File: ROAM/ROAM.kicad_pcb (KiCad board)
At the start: 4 copper layers, 90 x 56.8 mm, 26 parts, among them J1 CommanderX16Expansion Alt, SW1 SW_DIP_x04, U1 SST39SF040 (ROM), U2 74HCT00, U3 74HCT138, U4 AS6C4008 (RAM), U5 FM24C64B

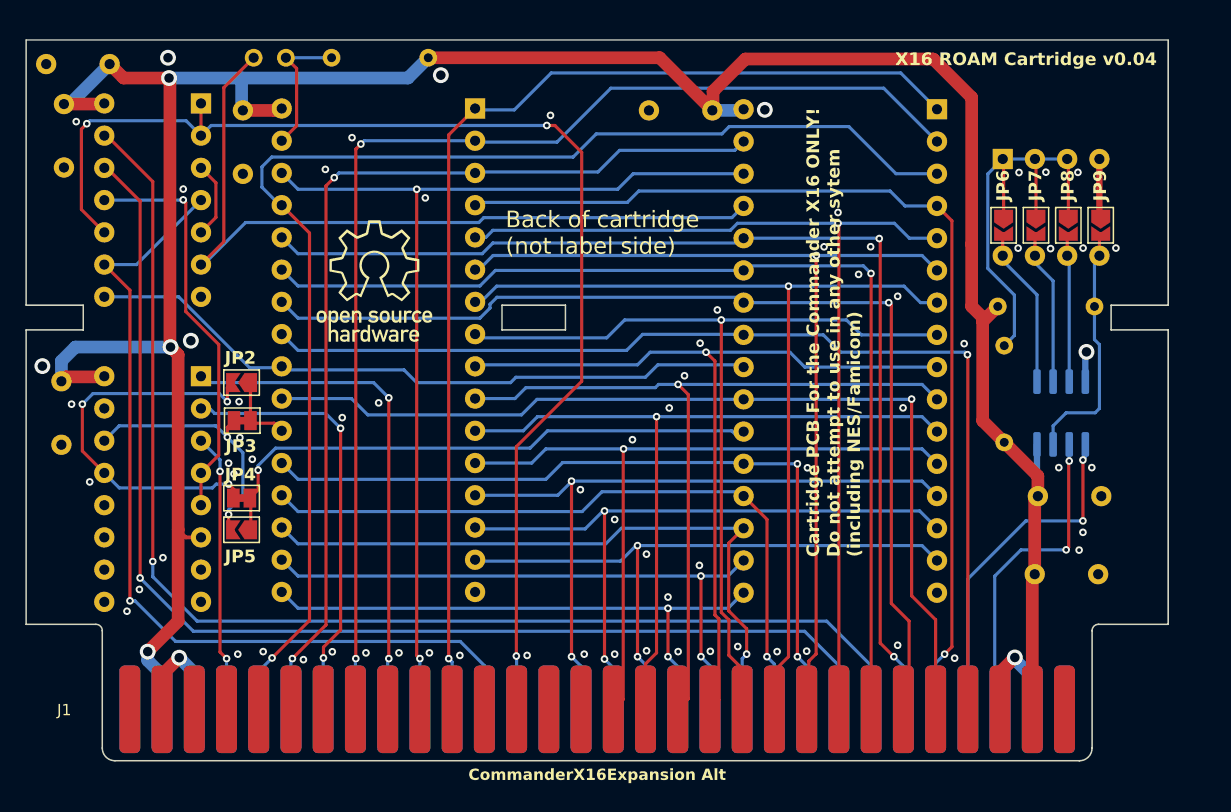
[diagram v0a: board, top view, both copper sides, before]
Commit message: Routed new layout with larger footprint keepout zones.
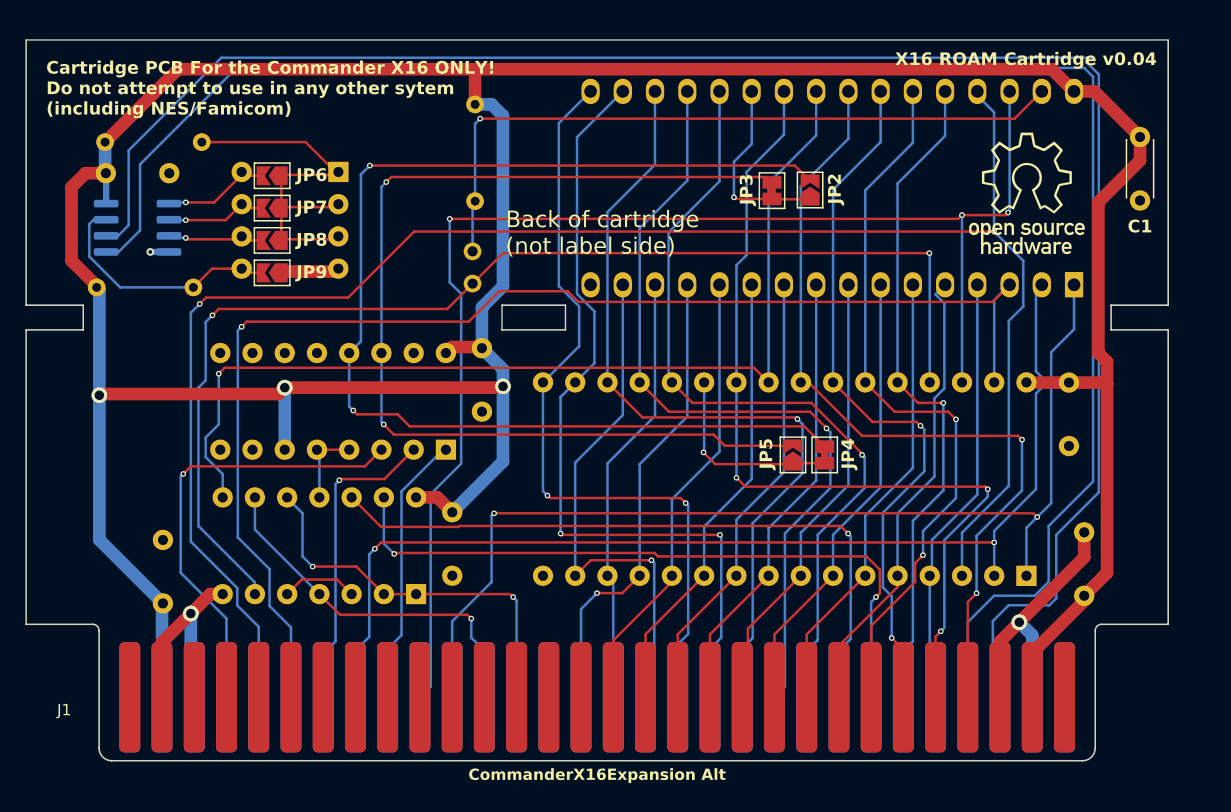
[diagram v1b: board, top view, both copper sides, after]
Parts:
- C1: moved to F.Cu
- U1: footprint Package_DIP:DIP-32_W15.24mm_Socket -> Socket:DIP_Socket-32_W11.9_W12.7_W15.24_W17.78_W18.5_3M_232-1285-00-0602J
- U2: footprint Package_DIP:DIP-14_W7.62mm_Socket -> Package_DIP:DIP-14_W7.62mm
- U3: footprint Package_DIP:DIP-16_W7.62mm_Socket -> Package_DIP:DIP-16_W7.62mm
- moved C7 89.7 mm to (130.8, 116.8), turned to -90 degrees
- moved C5 77.7 mm to (58.7, 88.5)
- moved R2 74.7 mm to (53.6, 86.0), turned to 0 degrees
- moved U5 74.2 mm to (56.2, 92.8), turned to 180 degrees
- moved C6 73.7 mm to (58.2, 117.4), turned to -90 degrees
- moved R3 71.0 mm to (60.6, 97.5)
- moved C1 70.7 mm to (135.2, 90.7)
- moved JP9 65.4 mm to (66.8, 96.3), turned to 180 degrees
- moved JP8 62.8 mm to (66.8, 93.8), turned to 180 degrees
- moved JP7 60.2 mm to (66.8, 91.2), turned to 180 degrees
- moved JP6 57.8 mm to (66.8, 88.7), turned to 180 degrees
- moved SW1 52.4 mm to (72.0, 88.4), turned to 180 degrees
- moved U1 49.2 mm to (130.0, 97.3), turned to 90 degrees
- moved JP2 47.3 mm to (109.2, 89.8), turned to 90 degrees
- moved JP4 46.1 mm to (110.3, 110.7), turned to -90 degrees
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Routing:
- net /SCL: track 25.0 -> 143.4 mm, vias 2 -> 0
- net /SDA: track 27.3 -> 142.0 mm, vias 2 -> 0
- net /RWB: track 98.9 -> 31.1 mm, vias 3 -> 2
- net +5V: track 211.7 -> 275.1 mm
- net Net-(JP2-B): track 31.1 -> 93.6 mm, vias 3 -> 2
- net Net-(JP3-A): track 20.6 -> 83.0 mm
- net /A14: track 99.2 -> 54.0 mm, vias 1 -> 2
- net Net-(JP1-B): track 11.0 -> 55.9 mm, vias 0 -> 1
- net A12: track 77.7 -> 34.3 mm, vias 1 -> 0
- net /PHI2: track 70.6 -> 29.1 mm
- net ROMB0: track 99.0 -> 140.1 mm, vias 1 -> 2
- net /A15: track 94.8 -> 53.7 mm
- net A7: track 75.7 -> 36.6 mm, vias 1 -> 0
- net A6: track 72.7 -> 36.0 mm, vias 1 -> 0
- net A5: track 70.8 -> 36.0 mm, vias 1 -> 0
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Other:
- outline, holes or cut-outs redrawn
- board text added: "NVRAM Addr 0x14 +"
- board text removed: "NVRAM Addr 0x50 +"

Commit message: Add ROM reverse polarity circuit; Gerber out 0.20
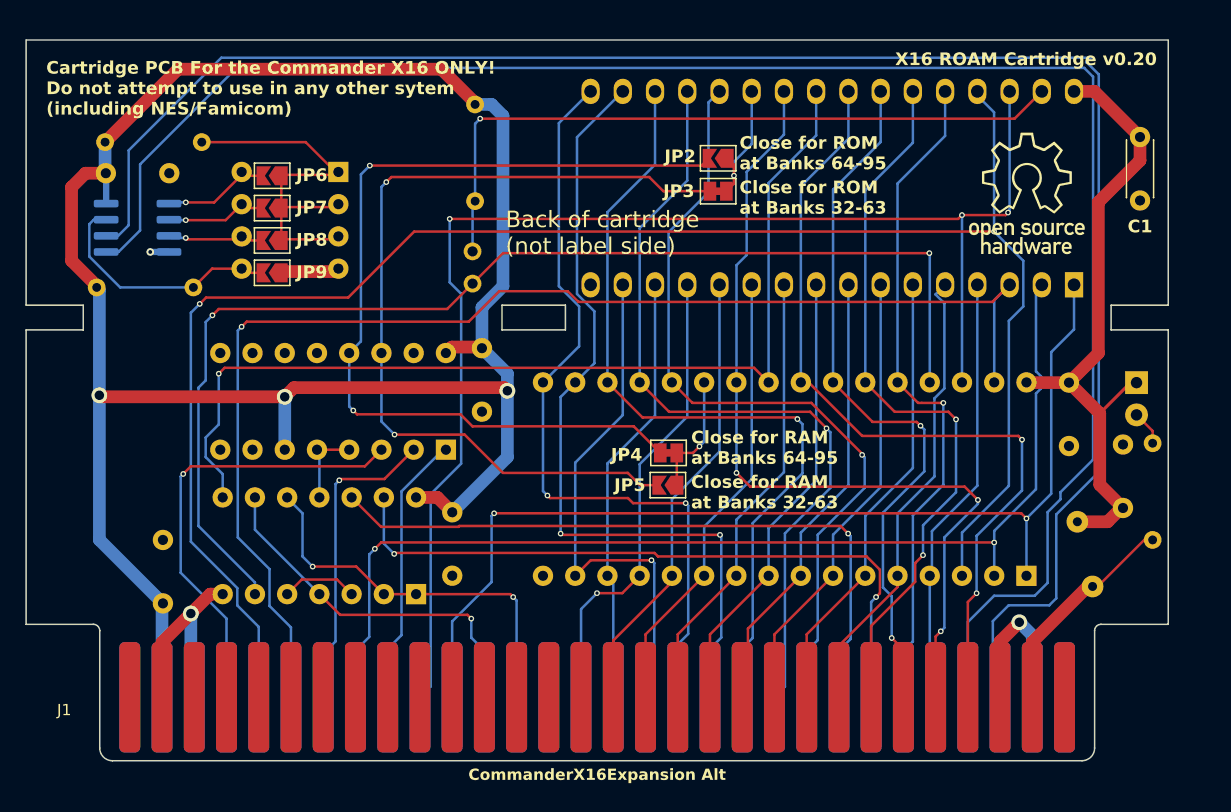
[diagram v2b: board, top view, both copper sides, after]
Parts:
- added D1: LED, LED_THT:LED_D3.0mm, B.Cu at (134.9, 105.0)
- added F1: Polyfuse_Small, Fuse:Fuse_Bourns_MF-RHT100, B.Cu at (130.3, 116.0)
- added R4: 4K7, Resistor_THT:R_Axial_DIN0204_L3.6mm_D1.6mm_P7.62mm_Horizontal, B.Cu at (136.2, 109.8)
- moved JP4 12.3 mm to (98.0, 110.5), turned to 0 degrees
- moved JP5 10.1 mm to (98.0, 113.1), turned to 180 degrees
- moved JP2 7.66 mm to (102.0, 87.3), turned to 180 degrees
- moved C7 7.57 mm to (133.9, 109.9)
- moved JP3 4.24 mm to (102.0, 89.9), turned to 0 degrees
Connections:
- C1 pad 2: +5V -> +5VD
- C4 pad 2: +5V -> +5VD
- C7 pad 2: +5V -> +5VD
- J1 pad 57: +5V -> Net-(F1-Pad2)
- U1 pad 32: +5V -> +5VD
- U4 pad 32: +5V -> +5VD
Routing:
- net +5V: track 275.1 -> 164.3 mm
- net +5VD: track 0.00 -> 51.3 mm
- net Net-(JP2-B): track 93.6 -> 72.7 mm
- net Net-(F1-Pad2): track 0.00 -> 17.2 mm
- net Net-(JP3-A): track 83.0 -> 69.1 mm
- net GND: track 45.6 -> 36.4 mm
- net !RAMBEN: track 15.5 -> 9.75 mm
- net !ROMBEN: track 15.0 -> 10.3 mm
- net Net-(D1-A): track 0.00 -> 2.76 mm
- net A10: track 70.3 -> 68.5 mm
- net ROMB4: track 83.3 -> 82.5 mm
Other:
- outline, holes or cut-outs redrawn
- board text added: "Close for RAM at Banks 32-63"
- board text added: "Close for RAM at Banks 64-95"
- board text added: "Close for ROM at Banks 32-63"
- board text added: "Close for ROM at Banks 64-95"
- board text added: "NVRAM Addr 0x50 +"
- board text added: "NVRAM Wr. Enable"
- board text added: "WARNING: SHUTDOWN AND ROTATE ROM WHEN LIT!"
- board text added: "X16 ROAM Cartridge v0.20"
- board text removed: "NVRAM Addr 0x14 +"
- board text removed: "NVRAM Wr. Prot."
- board text removed: "X16 ROAM Cartridge v0.04"
